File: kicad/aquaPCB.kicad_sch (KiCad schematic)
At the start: 0 parts

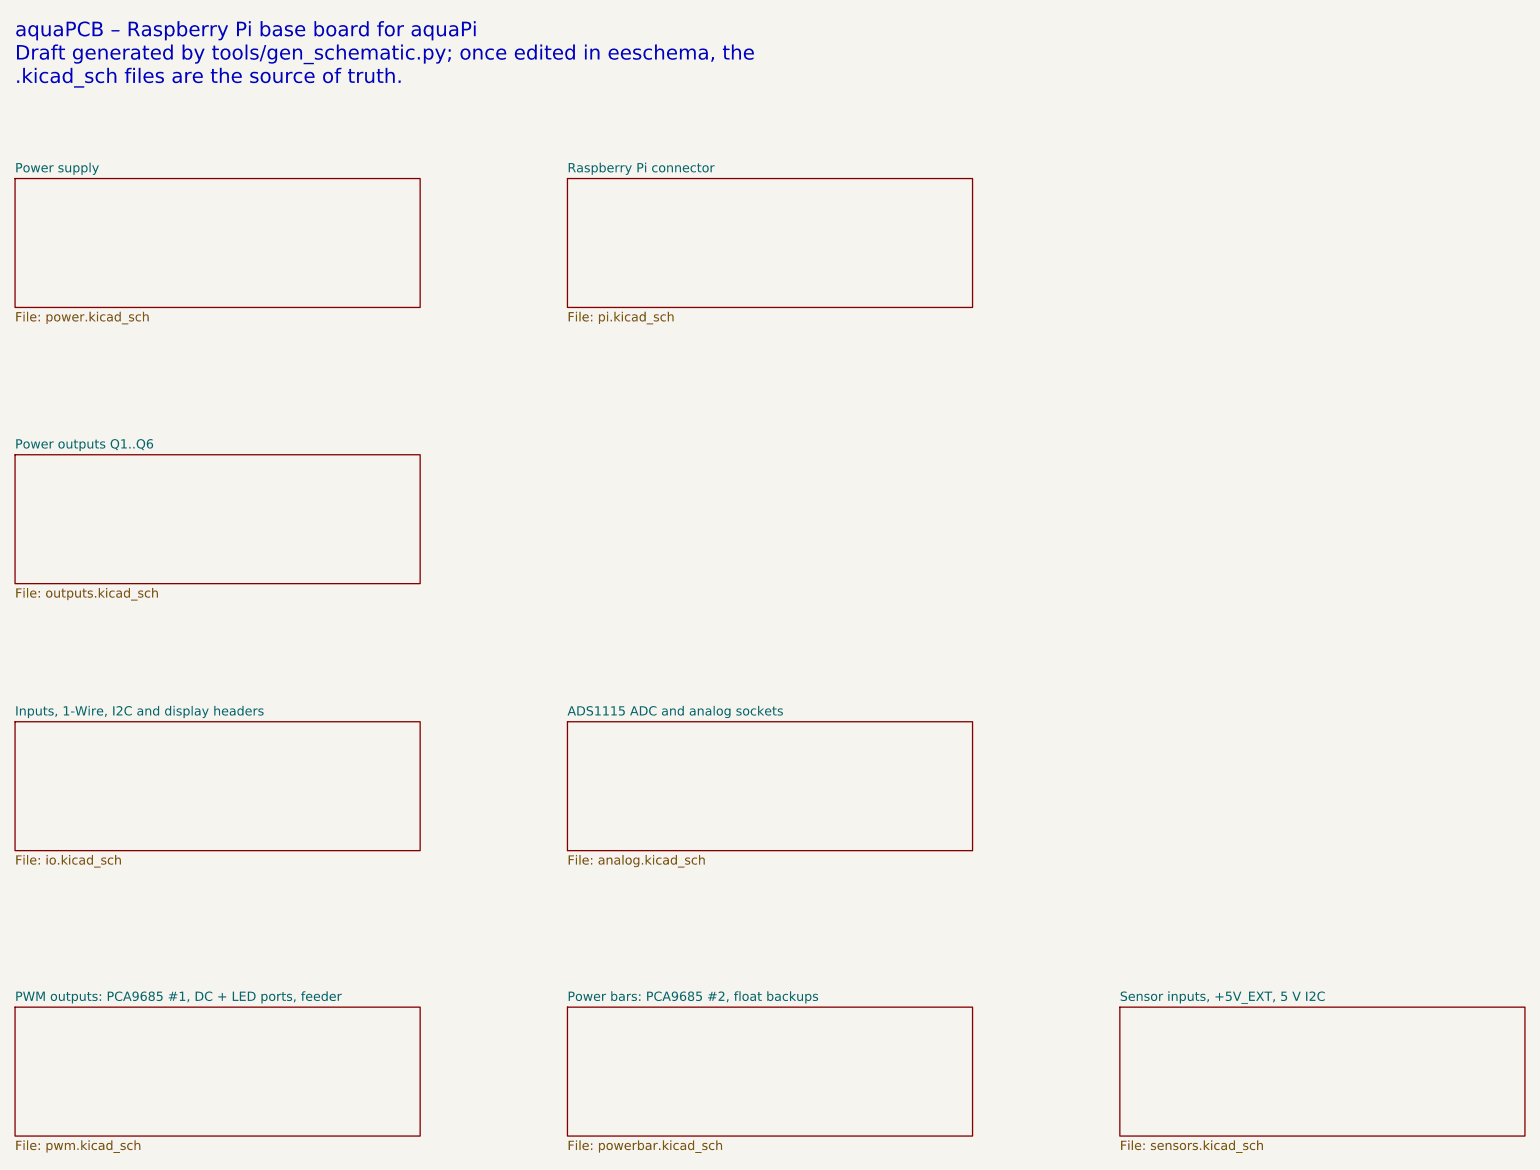
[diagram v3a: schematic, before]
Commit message: kicad: pin headers for 1-Wire, ADC and floats; connectivity-driven re-placement
J19, ADC sockets (J36/J37/J26/J27, 3x4 grid) and floats J30/J31 are pin headers now. All footprints placed on the board (big connectors first, flat parts allowed under the Pi, user-placed U10/RN5/J32/U11 and user routing kept): signal ratsnest 7824 -> 4450 mm, crossings 1776 -> 862. ERC 0, DRC copper 0, parity 0.

Co-Authored-By: Claude Opus 5.5 <noreply@anthropic.com>
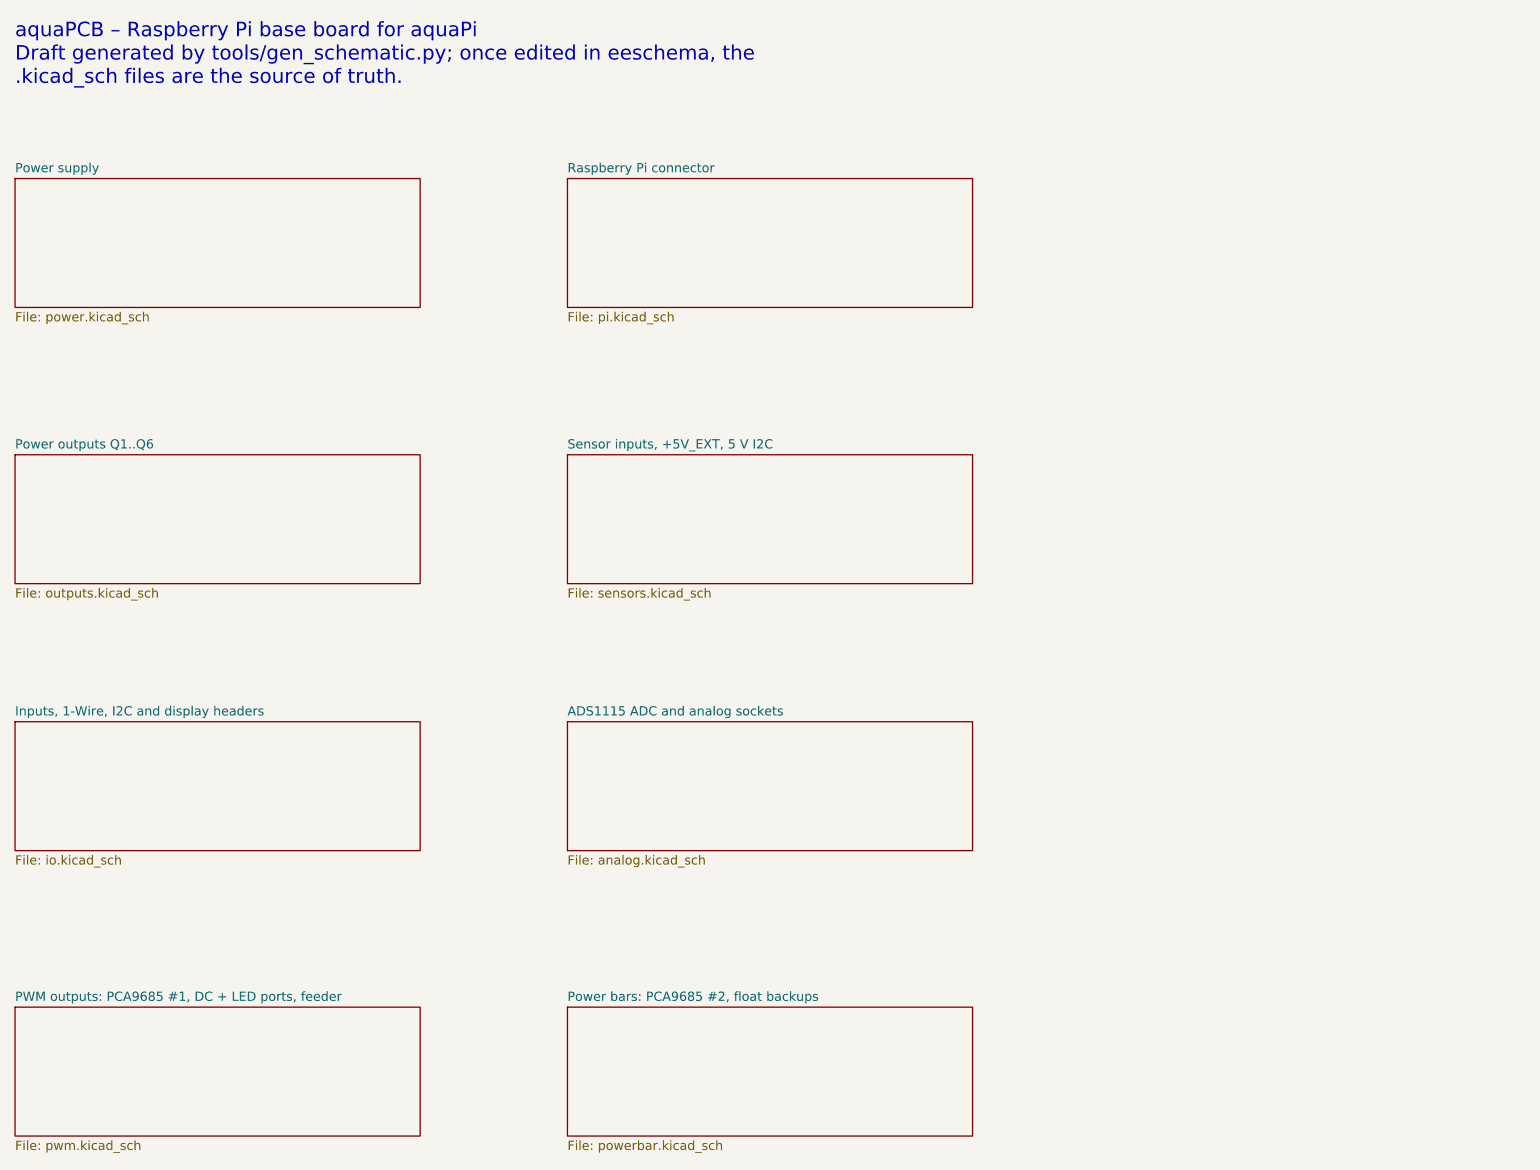
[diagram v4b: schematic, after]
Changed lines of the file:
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@@
+	)
+	(sheet
+		(at 106.68 152.4)
+		(size 55.88 17.78)
+		(exclude_from_sim no)
+		(in_bom yes)
+		(on_board yes)
+		(dnp no)
+		(fields_autoplaced yes)
+		(stroke
+			(width 0.1524)
+			(type solid)
+		)
+		(fill
+			(color 0 0 0 0)
+		)
+		(property "Sheetname" "Power bars: PCA9685 #2, float backups"
+			(at 106.68 151.688 0)
+			(show_name no)
+			(do_not_autoplace no)
+			(effects
+				(font
+					(size 1.27 1.27)
+				)
+				(justify left bottom)
+			)
+		)
+		(property "Sheetfile" "powerbar.kicad_sch"
+			(at 106.68 170.768 0)
+			(show_name no)
+			(do_not_autoplace no)
+			(effects
+				(font
+					(size 1.27 1.27)
+				)
+				(justify left top)
+			)
+		)
+		(instances
+			(project "aquaPCB"
+				(path "/80232f81-1179-4777-a7f0-674a974d53cc"
+					(page "8")
+				)
+			)
+		)
+	)
+	(sheet
+		(at 30.48 152.4)
+		(size 55.88 17.78)
+		(exclude_from_sim no)
+		(in_bom yes)
+		(on_board yes)
+		(dnp no)
+		(fields_autoplaced yes)
+		(stroke
+			(width 0.1524)
+			(type solid)
+		)
+		(fill
+			(color 0 0 0 0)
+		)
+		(property "Sheetname" "PWM outputs: PCA9685 #1, DC + LED ports, feeder"
+			(at 30.48 151.688 0)
+			(show_name no)
+			(do_not_autoplace no)
+			(effects
+				(font
+					(size 1.27 1.27)
+				)
+				(justify left bottom)
+			)
+		)
+		(property "Sheetfile" "pwm.kicad_sch"
+			(at 30.48 170.768 0)
+			(show_name no)
+			(do_not_autoplace no)
+			(effects
+				(font
+					(size 1.27 1.27)
+				)
+				(justify left top)
+			)
+		)
+		(instances
+			(project "aquaPCB"
+				(path "/80232f81-1179-4777-a7f0-674a974d53cc"
+					(page "7")
+				)
+			)
+		)
 	)
 	(sheet
@@
 	)
 	(sheet
+		(at 106.68 76.2)
+		(size 55.88 17.78)
+		(exclude_from_sim no)
+		(in_bom yes)
+		(on_board yes)
+		(dnp no)
+		(fields_autoplaced yes)
+		(stroke
+			(width 0.1524)
+			(type solid)
+		)
+		(fill
+			(color 0 0 0 0)
+		)
+		(property "Sheetname" "Sensor inputs, +5V_EXT, 5 V I2C"
+			(at 106.68 75.488 0)
+			(show_name no)
+			(do_not_autoplace no)
+			(effects
+				(font
+					(size 1.27 1.27)
+				)
+				(justify left bottom)
+			)
+		)
+		(property "Sheetfile" "sensors.kicad_sch"
+			(at 106.68 94.568 0)
+			(show_name no)
+			(do_not_autoplace no)
+			(effects
+				(font
+					(size 1.27 1.27)
+				)
+				(justify left top)
+			)
+		)
+		(instances
+			(project "aquaPCB"
+				(path "/80232f81-1179-4777-a7f0-674a974d53cc"
+					(page "9")
+				)
+			)
+		)
+	)
+	(sheet
 		(at 106.68 38.1)
 		(size 55.88 17.78)
@@
 				)
 			)
-		)
-	)
-	(sheet
-		(at 30.48 152.4)
-		(size 55.88 17.78)
-		(exclude_from_sim no)
-		(in_bom yes)
-		(on_board yes)
-		(dnp no)
-		(fields_autoplaced yes)
-		(stroke
-			(width 0.1524)
-			(type solid)
-		)
-		(fill
-			(color 0 0 0 0)
-		)
-		(property "Sheetname" "PWM outputs: PCA9685 #1, DC + LED ports, feeder"
-			(at 30.48 151.688 0)
-			(show_name no)
-			(do_not_autoplace no)
-			(effects
-				(font
-					(size 1.27 1.27)
-				)
-				(justify left bottom)
-			)
-		)
-		(property "Sheetfile" "pwm.kicad_sch"
-			(at 30.48 170.768 0)
-			(show_name no)
-			(do_not_autoplace no)
-			(effects
-				(font
-					(size 1.27 1.27)
-				)
-				(justify left top)
-			)
-		)
-		(instances
-			(project "aquaPCB"
-				(path "/80232f81-1179-4777-a7f0-674a974d53cc"
-					(page "7")
-				)
-			)
-		)
-	)
-	(sheet
-		(at 106.68 152.4)
-		(size 55.88 17.78)
-		(exclude_from_sim no)
-		(in_bom yes)
-		(on_board yes)
-		(dnp no)
-		(fields_autoplaced yes)
-		(stroke
-			(width 0.1524)
-			(type solid)
-		)
-		(fill
-			(color 0 0 0 0)
-		)
-		(property "Sheetname" "Power bars: PCA9685 #2, float backups"
-			(at 106.68 151.688 0)
-			(show_name no)
-			(do_not_autoplace no)
-			(effects
-				(font
-					(size 1.27 1.27)
-				)
-				(justify left bottom)
-			)
-		)
-		(property "Sheetfile" "powerbar.kicad_sch"
-			(at 106.68 170.768 0)
-			(show_name no)
-			(do_not_autoplace no)
-			(effects
-				(font
-					(size 1.27 1.27)
-				)
-				(justify left top)
-			)
-		)
-		(instances
-			(project "aquaPCB"
-				(path "/80232f81-1179-4777-a7f0-674a974d53cc"
-					(page "8")
-				)
-			)
-		)
-	)
-	(sheet
-		(at 182.88 152.4)
-		(size 55.88 17.78)
-		(exclude_from_sim no)
-		(in_bom yes)
-		(on_board yes)
-		(dnp no)
-		(fields_autoplaced yes)
-		(stroke
-			(width 0.1524)
-			(type solid)
-		)
-		(fill
-			(color 0 0 0 0)
-		)
-		(property "Sheetname" "Sensor inputs, +5V_EXT, 5 V I2C"
-			(at 182.88 151.688 0)
-			(show_name no)
-			(do_not_autoplace no)
-			(effects
-				(font
-					(size 1.27 1.27)
-				)
-				(justify left bottom)
-			)
-		)
-		(property "Sheetfile" "sensors.kicad_sch"
-			(at 182.88 170.768 0)
-			(show_name no)
-			(do_not_autoplace no)
-			(effects
-				(font
-					(size 1.27 1.27)
-				)
-				(justify left top)
-			)
-		)
-		(instances
-			(project "aquaPCB"
-				(path "/80232f81-1179-4777-a7f0-674a974d53cc"
-					(page "9")
-				)
-			)

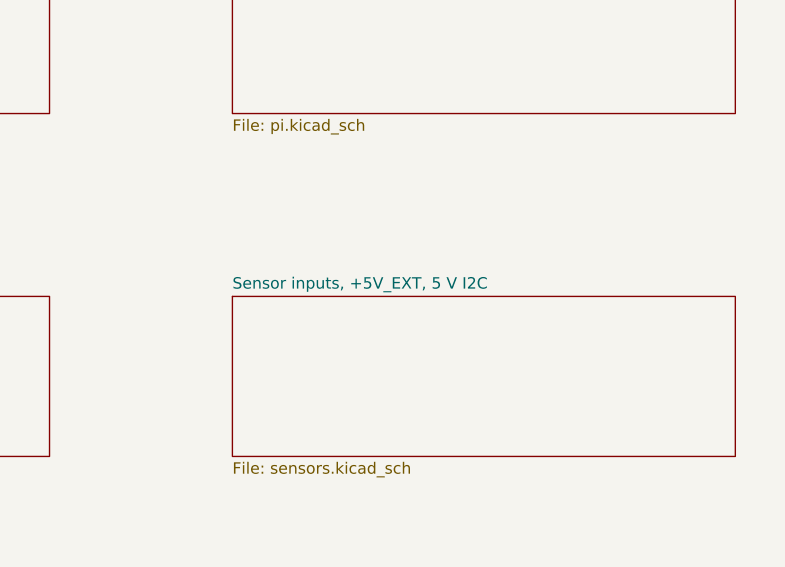
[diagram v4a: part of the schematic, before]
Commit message: kicad: power bar group re-placed and routed, 5 V I2C removed
- Power bars: U10 rotated, RN5..RN8 re-placed, J32/J33 rotated by 180 deg
  (pinout unchanged). Original PCA #2 channel order kept (bar 1 outlet n =
  ch n-1, bar 2 = ch n+7); identical array elements re-assigned in the
  schematic for routing. All power bar nets routed, U10 supply re-done,
  SDA/SCL escape stubs towards the Pi header.
- Sensors: 5 V I2C (PCA9306, J35) removed, I2C is 3.3 V only.
- Board: manual group placement and routing, Q4_DRV clearance fix,
  duplicate via and dangling GND stubs removed.
- README: 5 V I2C note and PCA #2 channel order / rotated headers.

Co-Authored-By: Claude Opus 5.5 <noreply@anthropic.com>
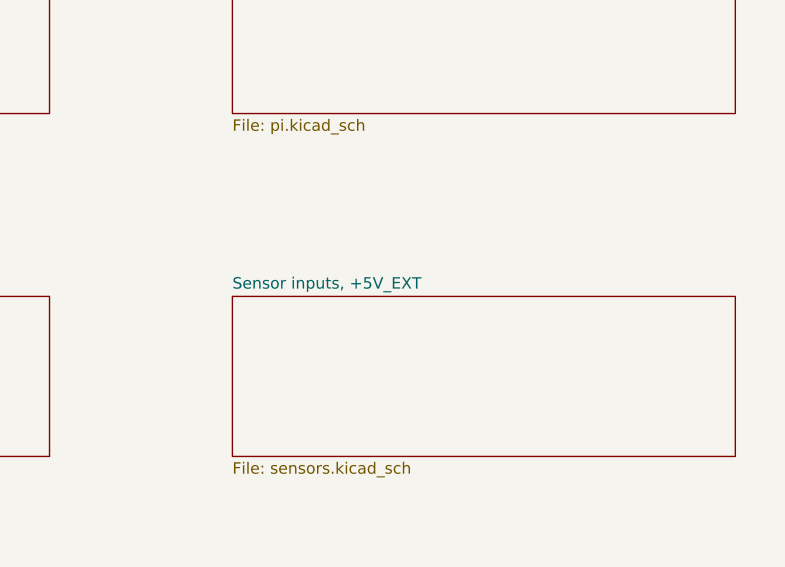
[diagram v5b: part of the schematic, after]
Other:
- sheet Sensor inputs, +5V_EXT, 5 V I2C renamed Sensor inputs, +5V_EXT
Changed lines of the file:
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@@
 			(color 0 0 0 0)
 		)
-		(property "Sheetname" "Sensor inputs, +5V_EXT, 5 V I2C"
+		(property "Sheetname" "Sensor inputs, +5V_EXT"
 			(at 106.68 75.488 0)
 			(show_name no)
